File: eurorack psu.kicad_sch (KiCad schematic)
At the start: 22 parts, among them J1 Screw Terminal 1x3, J2 Screw_Terminal_01x03, U1 LM7812_TO220, U2 LM7912_TO220

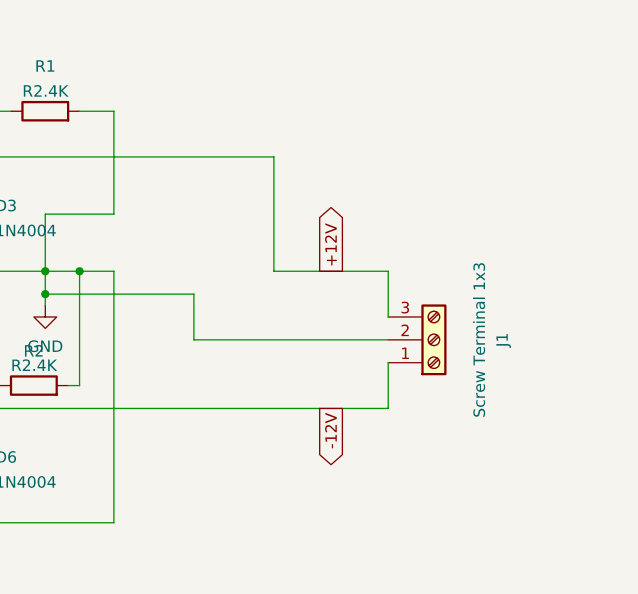
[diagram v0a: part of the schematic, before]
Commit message: added control LEDs
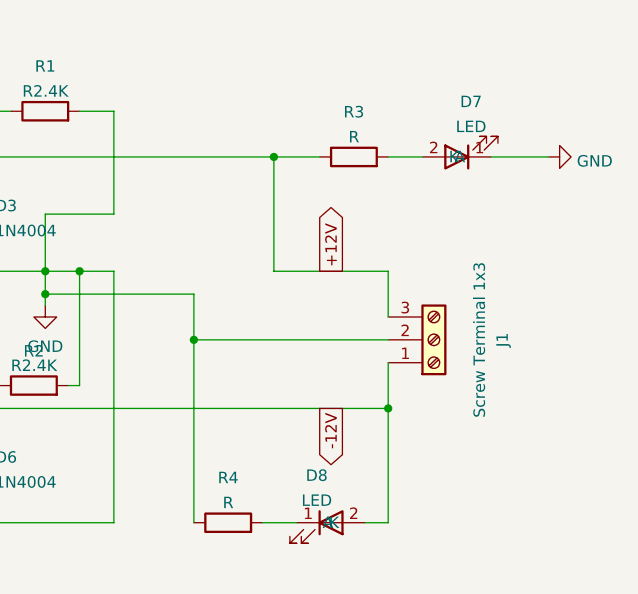
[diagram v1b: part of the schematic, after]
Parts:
- added D7, D8: LED, LED_THT:LED_D3.0mm, symbol Device:LED
- added R3, R4: R, Resistor_THT:R_Axial_DIN0207_L6.3mm_D2.5mm_P7.62mm_Horizontal, symbol Device:R
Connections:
- net +12V: now also R3.1
- net -12V: now also D8.2 (A)
- net GND: now also D7.1 (K), R4.1
- new net: D8.1 (K), R4.2
- new net: D7.2 (A), R3.2
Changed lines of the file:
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@@
   (junction (at 41.91 104.14) (diameter 0) (color 0 0 0 0)
   )
+  (junction (at 163.83 83.82) (diameter 0) (color 0 0 0 0)
+  )
   (junction (at 105.41 91.44) (diameter 0) (color 0 0 0 0)
   )
@@
   (junction (at 105.41 63.5) (diameter 0) (color 0 0 0 0)
   )
+  (junction (at 185.42 91.44) (diameter 0) (color 0 0 0 0)
+  )
   (junction (at 147.32 78.74) (diameter 0) (color 0 0 0 0)
   )
+  (junction (at 172.72 63.5) (diameter 0) (color 0 0 0 0)
+  )
   (junction (at 60.96 104.14) (diameter 0) (color 0 0 0 0)
   )
@@
     (stroke (width 0) (type default) (color 0 0 0 0))
   )
+  (wire (pts (xy 163.83 83.82) (xy 163.83 104.14))
+    (stroke (width 0) (type default) (color 0 0 0 0))
+  )
   (wire (pts (xy 139.7 76.2) (xy 129.54 76.2))
     (stroke (width 0) (type default) (color 0 0 0 0))
@@
     (stroke (width 0) (type default) (color 0 0 0 0))
   )
+  (wire (pts (xy 171.45 104.14) (xy 175.26 104.14))
+    (stroke (width 0) (type default) (color 0 0 0 0))
+  )
   (wire (pts (xy 120.65 54.61) (xy 129.54 54.61))
     (stroke (width 0) (type default) (color 0 0 0 0))
@@
     (stroke (width 0) (type default) (color 0 0 0 0))
   )
+  (wire (pts (xy 172.72 63.5) (xy 177.8 63.5))
+    (stroke (width 0) (type default) (color 0 0 0 0))
+  )
   (wire (pts (xy 105.41 76.2) (xy 116.84 76.2))
     (stroke (width 0) (type default) (color 0 0 0 0))
   )
+  (wire (pts (xy 196.85 63.5) (xy 203.2 63.5))
+    (stroke (width 0) (type default) (color 0 0 0 0))
+  )
   (wire (pts (xy 129.54 66.04) (xy 129.54 63.5))
     (stroke (width 0) (type default) (color 0 0 0 0))
@@
     (stroke (width 0) (type default) (color 0 0 0 0))
   )
+  (wire (pts (xy 182.88 104.14) (xy 185.42 104.14))
+    (stroke (width 0) (type default) (color 0 0 0 0))
+  )
   (wire (pts (xy 60.96 63.5) (xy 74.93 63.5))
+    (stroke (width 0) (type default) (color 0 0 0 0))
+  )
+  (wire (pts (xy 185.42 104.14) (xy 185.42 91.44))
+    (stroke (width 0) (type default) (color 0 0 0 0))
+  )
+  (wire (pts (xy 185.42 63.5) (xy 189.23 63.5))
     (stroke (width 0) (type default) (color 0 0 0 0))
   )
@@
     (pin "1")
   )
+  (symbol (lib_id "Device:R") (at 167.64 104.14 90) (unit 1)
+    (in_bom yes) (on_board yes) (fields_autoplaced)
+    (property "Reference" "R4" (id 0) (at 167.64 99.1575 90))
+    (property "Value" "R" (id 1) (at 167.64 101.9326 90))
+    (property "Footprint" "Resistor_THT:R_Axial_DIN0207_L6.3mm_D2.5mm_P7.62mm_Horizontal" (id 2) (at 167.64 105.918 90)
+      (effects (font (size 1.27 1.27)) hide)
+    )
+    (property "Datasheet" "~" (id 3) (at 167.64 104.14 0)
+      (effects (font (size 1.27 1.27)) hide)
+    )
+    (pin "1")
+    (pin "2")
+  )
   (symbol (lib_id "Device:C_Polarized") (at 105.41 97.79 180) (unit 1)
     (in_bom yes) (on_board yes)
@@
     (pin "3")
   )
+  (symbol (lib_id "power:GND") (at 203.2 63.5 90) (unit 1)
+    (in_bom yes) (on_board yes) (fields_autoplaced)
+    (property "Reference" "#PWR01" (id 0) (at 209.55 63.5 0)
+      (effects (font (size 1.27 1.27)) hide)
+    )
+    (property "Value" "GND" (id 1) (at 206.375 63.979 90)
+      (effects (font (size 1.27 1.27)) (justify right))
+    )
+    (property "Footprint" "" (id 2) (at 203.2 63.5 0)
+      (effects (font (size 1.27 1.27)) hide)
+    )
+    (property "Datasheet" "" (id 3) (at 203.2 63.5 0)
+      (effects (font (size 1.27 1.27)) hide)
+    )
+    (pin "1")
+  )
   (symbol (lib_id "Diode:1N4004") (at 50.8 63.5 180) (unit 1)
     (in_bom yes) (on_board yes) (fields_autoplaced)
@@
     (pin "2")
   )
+  (symbol (lib_id "Device:LED") (at 193.04 63.5 180) (unit 1)
+    (in_bom yes) (on_board yes) (fields_autoplaced)
+    (property "Reference" "D7" (id 0) (at 194.6275 57.3745 0))
+    (property "Value" "LED" (id 1) (at 194.6275 60.1496 0))
+    (property "Footprint" "LED_THT:LED_D3.0mm" (id 2) (at 193.04 63.5 0)
+      (effects (font (size 1.27 1.27)) hide)
+    )
+    (property "Datasheet" "~" (id 3) (at 193.04 63.5 0)
+      (effects (font (size 1.27 1.27)) hide)
+    )
+    (pin "1")
+    (pin "2")
+  )
   (symbol (lib_id "Device:C_Polarized") (at 90.17 97.79 180) (unit 1)
     (in_bom yes) (on_board yes)
@@
     )
     (property "Datasheet" "http://www.vishay.com/docs/88503/1n4001.pdf" (id 3) (at 139.7 69.85 0)
+      (effects (font (size 1.27 1.27)) hide)
+    )
+    (pin "1")
+    (pin "2")
+  )
+  (symbol (lib_name "LED_1") (lib_id "Device:LED") (at 179.07 104.14 0) (unit 1)
+    (in_bom yes) (on_board yes) (fields_autoplaced)
+    (property "Reference" "D8" (id 0) (at 177.4825 98.9035 0))
+    (property "Value" "LED" (id 1) (at 177.4825 101.6786 0))
+    (property "Footprint" "LED_THT:LED_D3.0mm" (id 2) (at 179.07 104.14 0)
+      (effects (font (size 1.27 1.27)) hide)
+    )
+    (property "Datasheet" "~" (id 3) (at 179.07 104.14 0)
       (effects (font (size 1.27 1.27)) hide)
     )
@@
   (symbol (lib_id "power:GND") (at 147.32 80.01 0) (unit 1)
     (in_bom yes) (on_board yes) (fields_autoplaced)
-    (property "Reference" "#PWR01" (id 0) (at 147.32 86.36 0)
+    (property "Reference" "#PWR02" (id 0) (at 147.32 86.36 0)
       (effects (font (size 1.27 1.27)) hide)
     )
@@
     (pin "1")
   )
+  (symbol (lib_id "Device:R") (at 181.61 63.5 90) (unit 1)
+    (in_bom yes) (on_board yes) (fields_autoplaced)
+    (property "Reference" "R3" (id 0) (at 181.61 58.5175 90))
+    (property "Value" "R" (id 1) (at 181.61 61.2926 90))
+    (property "Footprint" "Resistor_THT:R_Axial_DIN0207_L6.3mm_D2.5mm_P7.62mm_Horizontal" (id 2) (at 181.61 65.278 90)
+      (effects (font (size 1.27 1.27)) hide)
+    )
+    (property "Datasheet" "~" (id 3) (at 181.61 63.5 0)
+      (effects (font (size 1.27 1.27)) hide)
+    )
+    (pin "1")
+    (pin "2")
+  )
   (sheet_instances
     (path "/" (page "1"))
   )
   (symbol_instances
+    (path "/8dd418d4-186c-4f93-9e36-b382d207613a"
+      (reference "#PWR01") (unit 1) (value "GND") (footprint "")
+    )
     (path "/f6d63c80-b334-4c8a-8145-9615e7a14d94"
-      (reference "#PWR01") (unit 1) (value "GND") (footprint "")
+      (reference "#PWR02") (unit 1) (value "GND") (footprint "")
     )
     (path "/357b0474-a690-4e4a-bbf4-280735c0576c"
@@
       (reference "D6") (unit 1) (value "1N4004") (footprint "Diode_THT:D_DO-41_SOD81_P10.16mm_Horizontal")
     )
+    (path "/a9486174-81a2-4d91-abca-4430c153b7d8"
+      (reference "D7") (unit 1) (value "LED") (footprint "LED_THT:LED_D3.0mm")
+    )
+    (path "/af76c2a5-33a6-4b98-b039-12b91d8ddb19"
+      (reference "D8") (unit 1) (value "LED") (footprint "LED_THT:LED_D3.0mm")
+    )
     (path "/89c0b3c3-0e63-4d05-a0e5-f4b35f6fa5ec"
       (reference "J1") (unit 1) (value "Screw Terminal 1x3") (footprint "TerminalBlock:TerminalBlock_bornier-3_P5.08mm")
@@
       (reference "R2") (unit 1) (value "R2.4K") (footprint "Resistor_THT:R_Axial_DIN0207_L6.3mm_D2.5mm_P7.62mm_Horizontal")
     )
+    (path "/fa309369-28f1-4e35-9688-c2cc9b3d2b38"
+      (reference "R3") (unit 1) (value "R") (footprint "Resistor_THT:R_Axial_DIN0207_L6.3mm_D2.5mm_P7.62mm_Horizontal")
+    )
+    (path "/395194f6-a89d-4beb-838a-3ef92eda17c0"
+      (reference "R4") (unit 1) (value "R") (footprint "Resistor_THT:R_Axial_DIN0207_L6.3mm_D2.5mm_P7.62mm_Horizontal")
+    )
     (path "/f53a921a-4e80-4c9f-bbf9-b32031a4aaab"

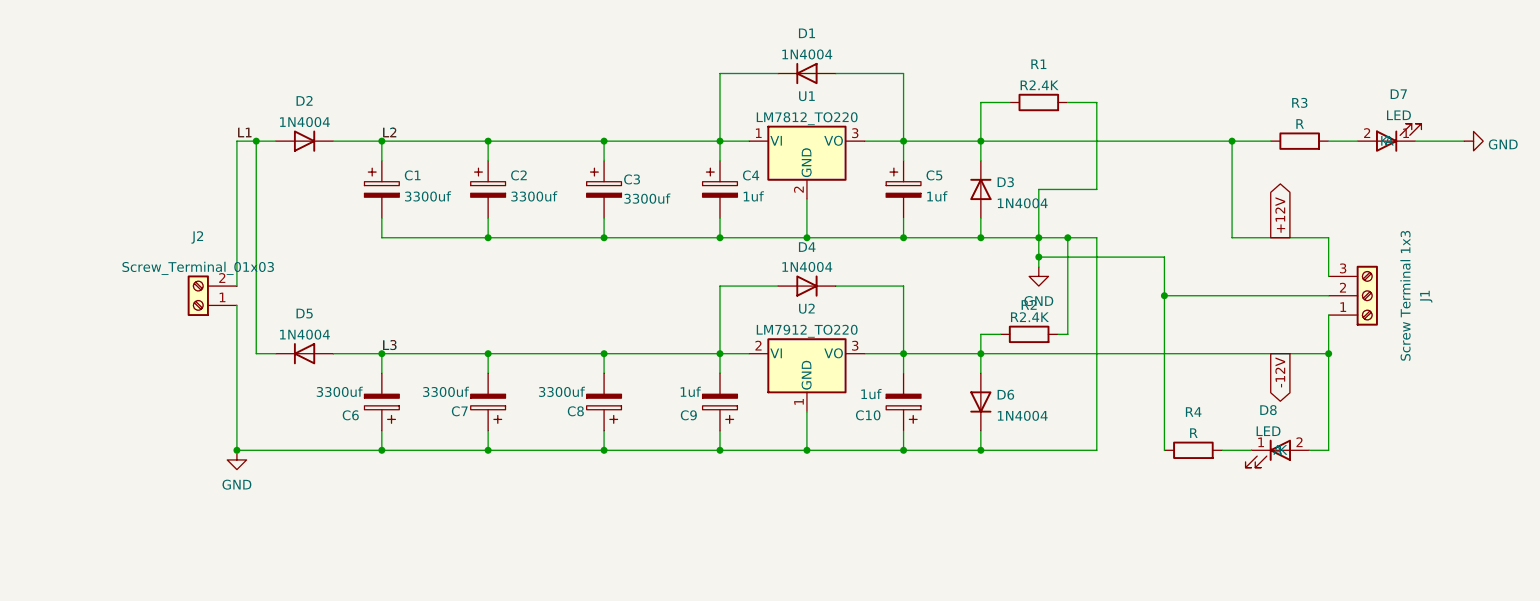
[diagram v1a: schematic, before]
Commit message: added PWR_FLAG to clear ERC errors
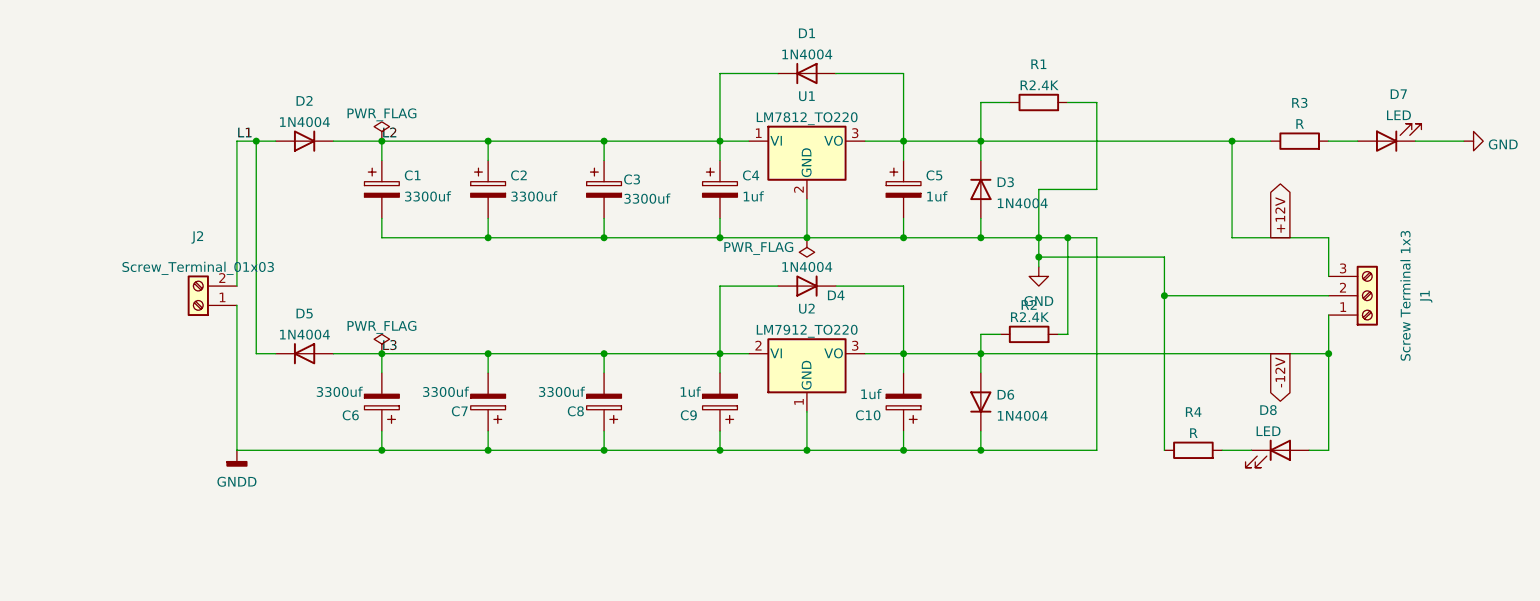
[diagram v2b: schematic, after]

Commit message: updated to full bridge
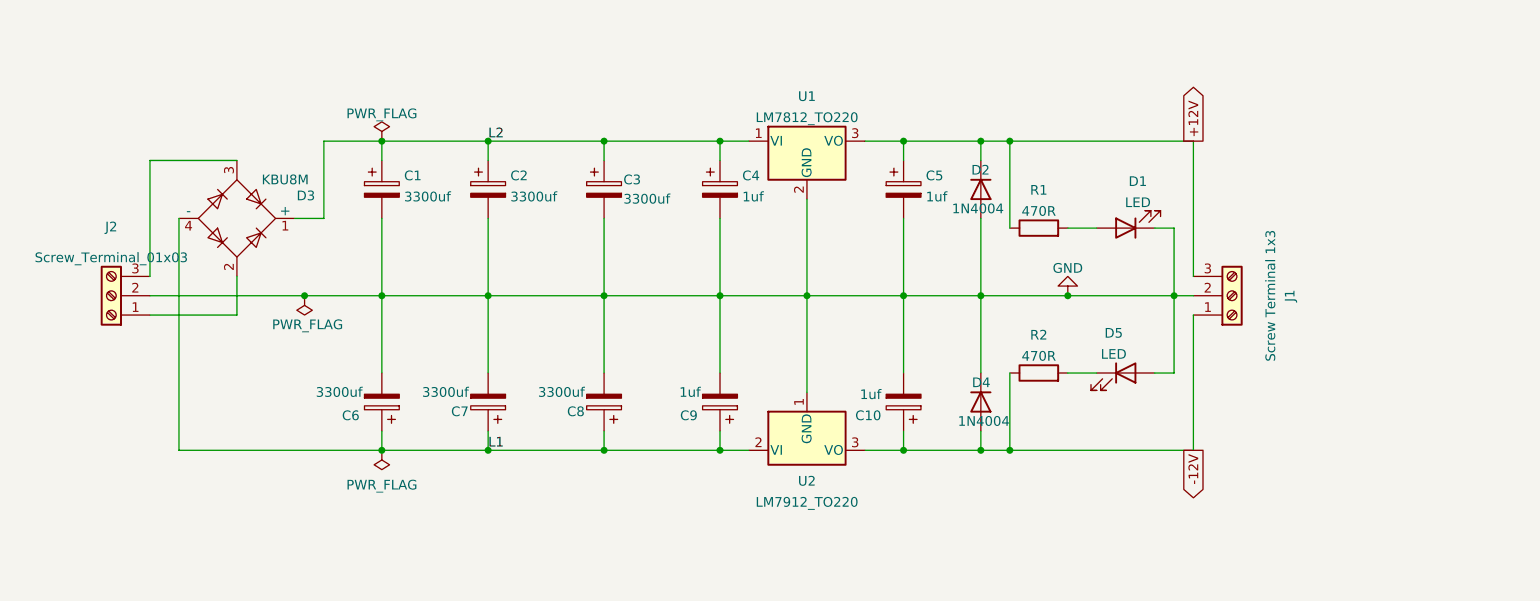
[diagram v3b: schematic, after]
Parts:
- removed D1, D2, D4, D5: 1N4004, Diode_THT:D_DO-41_SOD81_P10.16mm_Horizontal, symbol Diode:1N4004
- removed R1, R2: R2.4K, Resistor_THT:R_Axial_DIN0207_L6.3mm_D2.5mm_P7.62mm_Horizontal, symbol Device:R
- added D3: KBU8M, Diode_THT:Diode_Bridge_Vishay_KBU, symbol Diode_Bridge:KBU8M
- J1: footprint TerminalBlock:TerminalBlock_bornier-3_P5.08mm -> TerminalBlock_XINYA:TerminalBlock_XINYA_XY301-1x3-P5.00mm
- J2: footprint TerminalBlock:TerminalBlock_bornier-2_P5.08mm -> TerminalBlock_XINYA:TerminalBlock_XINYA_XY301-1x3-P5.00mm; symbol Connector:Screw_Terminal_01x02 -> Connector:Screw_Terminal_01x03
- R1: renamed from R3; value R -> 470R
- R2: renamed from R4; value R -> 470R
- renumbered D7 to D1, D3 to D2, D6 to D4, D8 to D5
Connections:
- net -12V: now also C10.1, R2.1; no longer C10.2, D5.2 (A)
- net GND: now also C10.2, C6.2, C7.2, C8.2, C9.2, D5.2 (A), J2.2 (Pin_2); no longer C10.1, C6.1, C7.1, C8.1, C9.1, J2.1 (Pin_1), R2.1
- net L1: now also C6.1, C7.1, C8.1, C9.1, U2.2 (VI), D3.4 (-); no longer J2.2 (Pin_2)
- net L2: now also D3.1 (+)
- removed net L3: C6.2, C7.2, C8.2, C9.2, U2.2 (VI)
- new net: D3.2, J2.1 (Pin_1)
- new net: D3.3, J2.3 (Pin_3)
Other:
- moved on the sheet: D1, D4, D5, J1, R1, R2, U2

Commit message: added protection diode for 78xx & 79xx, corrected orientation of some parts
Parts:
- added D6, D7: 1N4004, Diode_THT:D_DO-41_SOD81_P10.16mm_Horizontal, symbol Diode:1N4004
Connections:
- net +12V: now also D6.2 (A)
- net -12V: now also C10.2, D7.1 (K); no longer C10.1
- net GND: now also C10.1, C6.1, C7.1, C8.1, C9.1, D1.2 (A), D5.1 (K); no longer C10.2, C6.2, C7.2, C8.2, C9.2, D1.1 (K), D5.2 (A)
- net L1: now also C6.2, C7.2, C8.2, C9.2, D7.2 (A); no longer C6.1, C7.1, C8.1, C9.1
- net L2: now also D6.1 (K)
- net at R2.2: now also D5.2 (A); no longer D5.1 (K)
- net at R1.2: now also D1.1 (K); no longer D1.2 (A)
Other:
- moved on the sheet: C10, C6, C7, C8, C9, D1, D5

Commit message: Updated parts placement
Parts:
- removed D6, D7: 1N4004, Diode_THT:D_DO-41_SOD81_P10.16mm_Horizontal, symbol Diode:1N4004
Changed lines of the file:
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@@
   (junction (at 139.7 83.82) (diameter 0) (color 0 0 0 0)
   )
-  (wire (pts (xy 129.54 114.3) (xy 129.54 104.14))
-    (stroke (width 0) (type default) (color 0 0 0 0))
-  )
   (wire (pts (xy 129.54 83.82) (xy 139.7 83.82))
     (stroke (width 0) (type default) (color 0 0 0 0))
@@
     (stroke (width 0) (type default) (color 0 0 0 0))
   )
-  (wire (pts (xy 105.41 53.34) (xy 105.41 63.5))
-    (stroke (width 0) (type default) (color 0 0 0 0))
-  )
   (wire (pts (xy 53.34 63.5) (xy 60.96 63.5))
     (stroke (width 0) (type default) (color 0 0 0 0))
   )
-  (wire (pts (xy 113.03 53.34) (xy 105.41 53.34))
-    (stroke (width 0) (type default) (color 0 0 0 0))
-  )
   (wire (pts (xy 60.96 73.66) (xy 60.96 83.82))
     (stroke (width 0) (type default) (color 0 0 0 0))
@@
     (stroke (width 0) (type default) (color 0 0 0 0))
   )
-  (wire (pts (xy 113.03 114.3) (xy 105.41 114.3))
-    (stroke (width 0) (type default) (color 0 0 0 0))
-  )
   (wire (pts (xy 116.84 83.82) (xy 129.54 83.82))
     (stroke (width 0) (type default) (color 0 0 0 0))
@@
     (stroke (width 0) (type default) (color 0 0 0 0))
   )
-  (wire (pts (xy 120.65 114.3) (xy 129.54 114.3))
-    (stroke (width 0) (type default) (color 0 0 0 0))
-  )
   (wire (pts (xy 90.17 73.66) (xy 90.17 83.82))
     (stroke (width 0) (type default) (color 0 0 0 0))
   )
-  (wire (pts (xy 105.41 114.3) (xy 105.41 104.14))
-    (stroke (width 0) (type default) (color 0 0 0 0))
-  )
   (wire (pts (xy 60.96 83.82) (xy 74.93 83.82))
     (stroke (width 0) (type default) (color 0 0 0 0))
@@
     (stroke (width 0) (type default) (color 0 0 0 0))
   )
-  (wire (pts (xy 129.54 53.34) (xy 129.54 63.5))
-    (stroke (width 0) (type default) (color 0 0 0 0))
-  )
   (wire (pts (xy 74.93 104.14) (xy 90.17 104.14))
     (stroke (width 0) (type default) (color 0 0 0 0))
@@
   )
   (wire (pts (xy 49.53 73.66) (xy 53.34 73.66))
-    (stroke (width 0) (type default) (color 0 0 0 0))
-  )
-  (wire (pts (xy 120.65 53.34) (xy 129.54 53.34))
     (stroke (width 0) (type default) (color 0 0 0 0))
   )
@@
     (pin "3")
   )
-  (symbol (lib_id "Diode:1N4004") (at 116.84 114.3 180) (unit 1)
-    (in_bom yes) (on_board yes)
-    (property "Reference" "D7" (id 0) (at 118.11 120.65 0)
-      (effects (font (size 1.27 1.27)) (justify left))
-    )
-    (property "Value" "1N4004" (id 1) (at 120.65 118.11 0)
-      (effects (font (size 1.27 1.27)) (justify left))
-    )
-    (property "Footprint" "Diode_THT:D_DO-41_SOD81_P10.16mm_Horizontal" (id 2) (at 116.84 109.855 0)
-      (effects (font (size 1.27 1.27)) hide)
-    )
-    (property "Datasheet" "http://www.vishay.com/docs/88503/1n4001.pdf" (id 3) (at 116.84 114.3 0)
-      (effects (font (size 1.27 1.27)) hide)
-    )
-    (pin "1")
-    (pin "2")
-  )
   (symbol (lib_id "power:PWR_FLAG") (at 60.96 63.5 0) (unit 1)
     (in_bom yes) (on_board yes) (fields_autoplaced)
@@
     (pin "3")
   )
-  (symbol (lib_id "Diode:1N4004") (at 116.84 53.34 0) (unit 1)
-    (in_bom yes) (on_board yes)
-    (property "Reference" "D6" (id 0) (at 115.57 48.26 0)
-      (effects (font (size 1.27 1.27)) (justify left))
-    )
-    (property "Value" "1N4004" (id 1) (at 113.03 50.8 0)
-      (effects (font (size 1.27 1.27)) (justify left))
-    )
-    (property "Footprint" "Diode_THT:D_DO-41_SOD81_P10.16mm_Horizontal" (id 2) (at 116.84 57.785 0)
-      (effects (font (size 1.27 1.27)) hide)
-    )
-    (property "Datasheet" "http://www.vishay.com/docs/88503/1n4001.pdf" (id 3) (at 116.84 53.34 0)
-      (effects (font (size 1.27 1.27)) hide)
-    )
-    (pin "1")
-    (pin "2")
-  )
   (symbol (lib_id "Diode:1N4004") (at 139.7 97.79 270) (unit 1)
     (in_bom yes) (on_board yes)
@@
       (reference "D5") (unit 1) (value "LED") (footprint "LED_THT:LED_D3.0mm")
     )
-    (path "/edaf969f-353e-44bd-9eea-e5dbfe1f2308"
-      (reference "D6") (unit 1) (value "1N4004") (footprint "Diode_THT:D_DO-41_SOD81_P10.16mm_Horizontal")
-    )
-    (path "/5c2379a9-3f3c-41c8-b2c1-13dd0d7eda39"
-      (reference "D7") (unit 1) (value "1N4004") (footprint "Diode_THT:D_DO-41_SOD81_P10.16mm_Horizontal")
-    )
     (path "/89c0b3c3-0e63-4d05-a0e5-f4b35f6fa5ec"
